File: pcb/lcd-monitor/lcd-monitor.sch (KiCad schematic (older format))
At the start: 51 parts

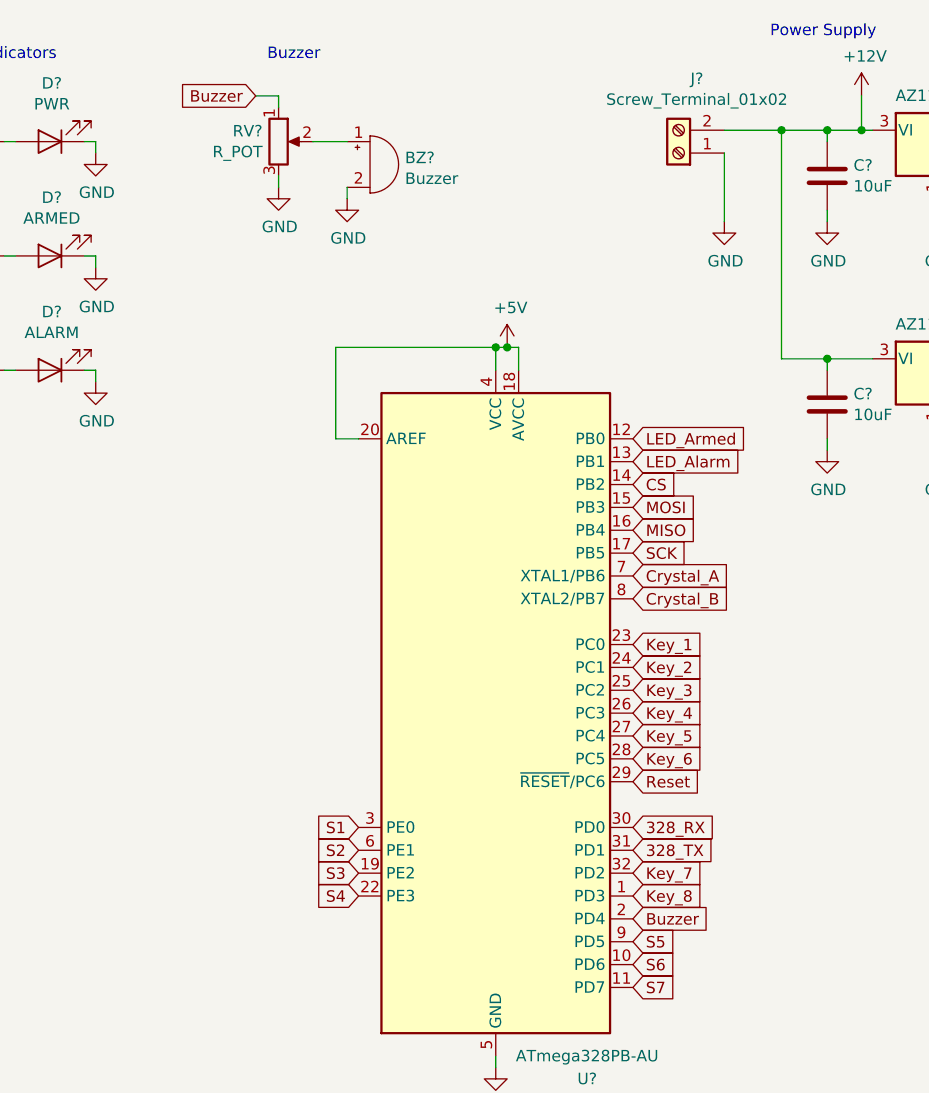
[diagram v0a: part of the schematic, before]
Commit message: Buzzer through PWM
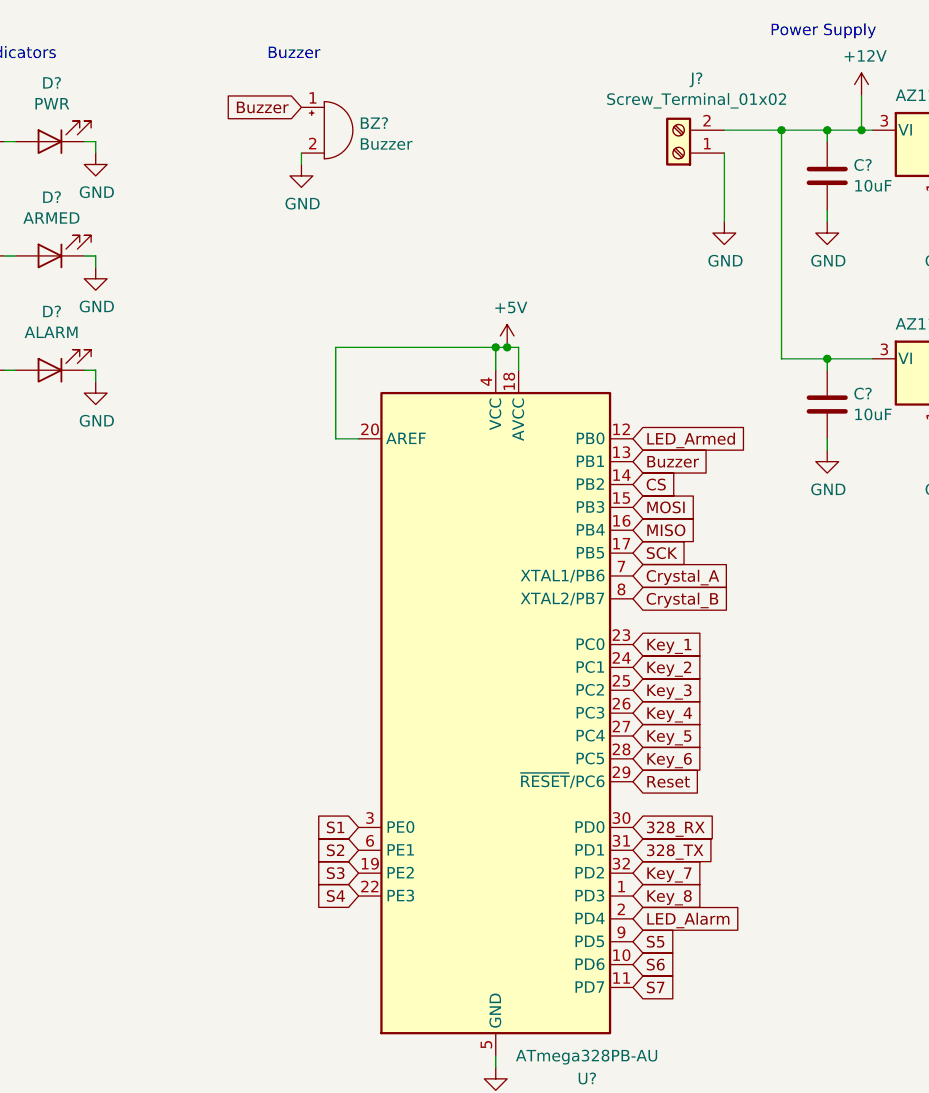
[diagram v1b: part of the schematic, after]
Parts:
- removed RV?: R_POT, symbol Device:R_POT
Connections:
- net Buzzer: now also BZ?.1 (-), U?.13 (PB1); no longer U?.2 (PD4)
- net LED_Alarm: now also U?.2 (PD4); no longer U?.13 (PB1)
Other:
- moved on the sheet: BZ?
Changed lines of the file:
@@
 Text GLabel 6350 2400 2    50   Input ~ 0
 LED_Armed
-Text GLabel 6350 2500 2    50   Input ~ 0
+Text GLabel 6350 4500 2    50   Input ~ 0
 LED_Alarm
 $Comp
 L Device:Buzzer BZ?
 U 1 1 5BD13CCE
-P 5200 1200
-F 0 "BZ?" H 5353 1229 50  0000 L CNN
-F 1 "Buzzer" H 5353 1138 50  0000 L CNN
-F 2 "" V 5175 1300 50  0001 C CNN
-F 3 "~" V 5175 1300 50  0001 C CNN
-	1    5200 1200
-	1    0    0    -1
-$EndComp
-$Comp
-L Device:R_POT RV?
-U 1 1 5BD13EFC
-P 4800 1100
-F 0 "RV?" H 4730 1146 50  0000 R CNN
-F 1 "R_POT" H 4730 1055 50  0000 R CNN
-F 2 "" H 4800 1100 50  0001 C CNN
-F 3 "~" H 4800 1100 50  0001 C CNN
-	1    4800 1100
+P 5000 1050
+F 0 "BZ?" H 5153 1079 50  0000 L CNN
+F 1 "Buzzer" H 5153 988 50  0000 L CNN
+F 2 "" V 4975 1150 50  0001 C CNN
+F 3 "~" V 4975 1150 50  0001 C CNN
+	1    5000 1050
 	1    0    0    -1
 $EndComp
 Text Notes 4750 750  0    50   ~ 0
 Buzzer
-Wire Wire Line
-	4800 950  4800 900
-Wire Wire Line
-	4950 1100 5100 1100
 $Comp
 L power:GND #PWR?
 U 1 1 5BD31A45
-P 5100 1350
-F 0 "#PWR?" H 5100 1100 50  0001 C CNN
-F 1 "GND" H 5105 1177 50  0000 C CNN
-F 2 "" H 5100 1350 50  0001 C CNN
-F 3 "" H 5100 1350 50  0001 C CNN
-	1    5100 1350
-	1    0    0    -1
-$EndComp
-$Comp
-L power:GND #PWR?
-U 1 1 5BD31A8A
-P 4800 1300
-F 0 "#PWR?" H 4800 1050 50  0001 C CNN
-F 1 "GND" H 4805 1127 50  0000 C CNN
-F 2 "" H 4800 1300 50  0001 C CNN
-F 3 "" H 4800 1300 50  0001 C CNN
-	1    4800 1300
+P 4900 1200
+F 0 "#PWR?" H 4900 950 50  0001 C CNN
+F 1 "GND" H 4905 1027 50  0000 C CNN
+F 2 "" H 4900 1200 50  0001 C CNN
+F 3 "" H 4900 1200 50  0001 C CNN
+	1    4900 1200
 	1    0    0    -1
 $EndComp
 Wire Wire Line
-	4800 1300 4800 1250
-Wire Wire Line
-	5100 1350 5100 1300
-Text GLabel 4700 900  0    50   Input ~ 0
+	4900 1200 4900 1150
+Text GLabel 4900 950  0    50   Input ~ 0
 Buzzer
-Wire Wire Line
-	4700 900  4800 900
-Text GLabel 6350 4500 2    50   Input ~ 0
+Text GLabel 6350 2500 2    50   Input ~ 0
 Buzzer
 NoConn ~ 2050 1100

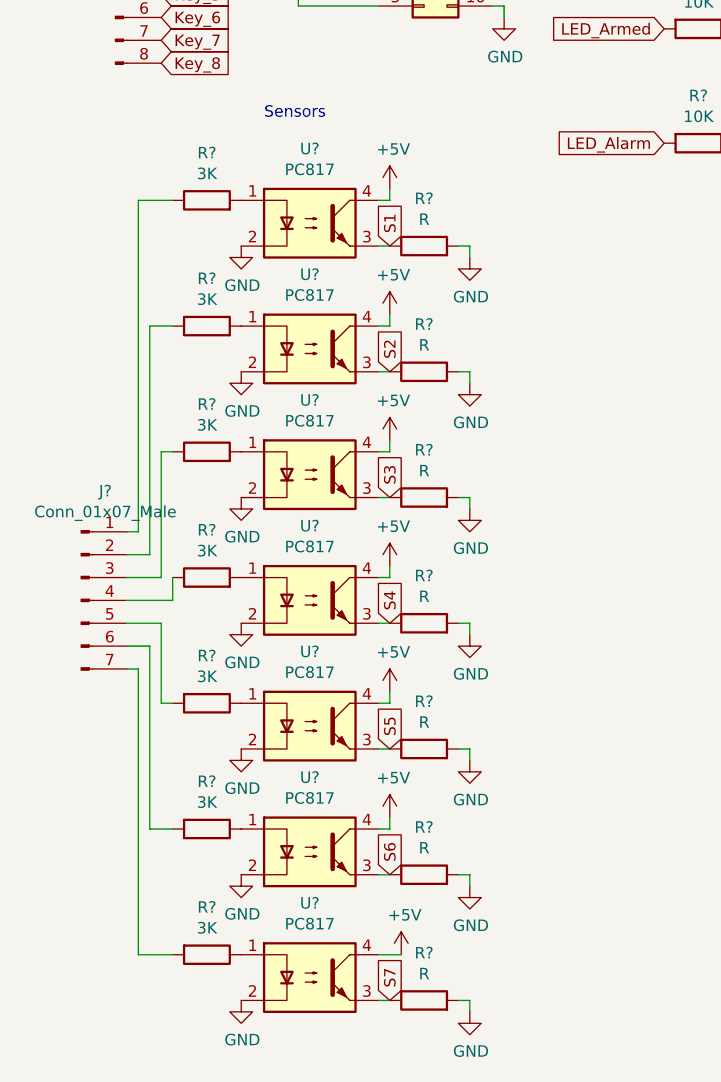
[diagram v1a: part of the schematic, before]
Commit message: Fix Optocoupler Resistor Values
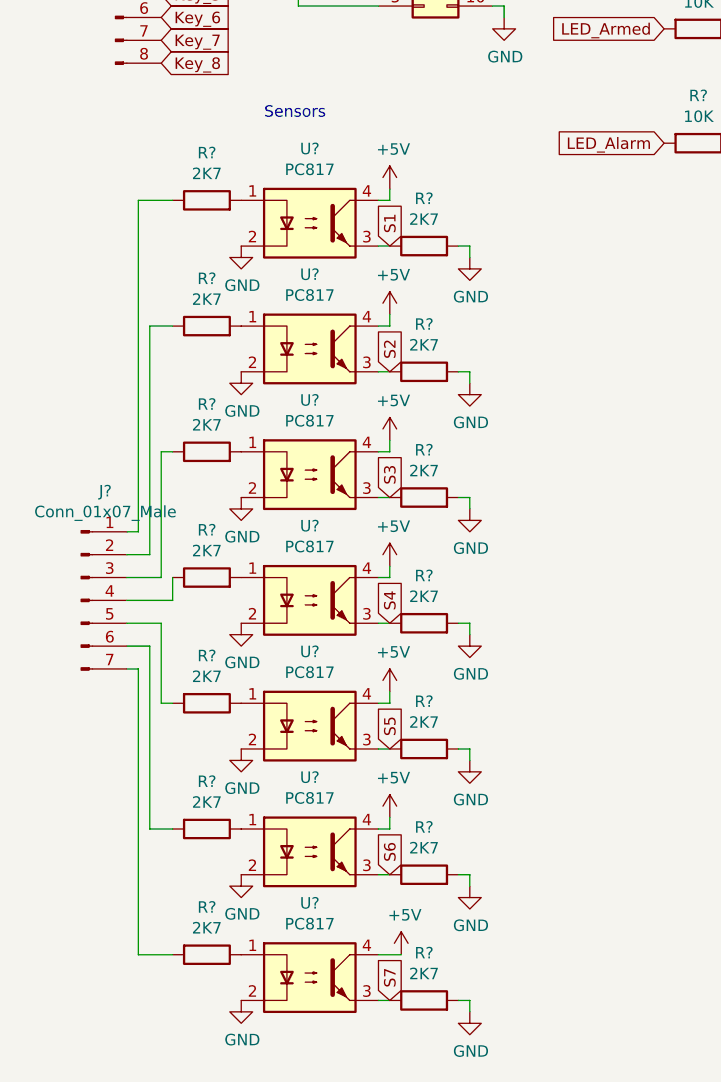
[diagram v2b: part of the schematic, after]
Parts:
- R? (x7): value R -> 2K7
- R? (x7): value 3K -> 2K7
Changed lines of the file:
@@
 P 2250 5850
 F 0 "R?" V 2457 5850 50  0000 C CNN
-F 1 "R" V 2366 5850 50  0000 C CNN
+F 1 "2K7" V 2366 5850 50  0000 C CNN
 F 2 "" V 2180 5850 50  0001 C CNN
 F 3 "~" H 2250 5850 50  0001 C CNN
@@
 P 2250 5300
 F 0 "R?" V 2457 5300 50  0000 C CNN
-F 1 "R" V 2366 5300 50  0000 C CNN
+F 1 "2K7" V 2366 5300 50  0000 C CNN
 F 2 "" V 2180 5300 50  0001 C CNN
 F 3 "~" H 2250 5300 50  0001 C CNN
@@
 P 1300 5650
 F 0 "R?" V 1093 5650 50  0000 C CNN
-F 1 "3K" V 1184 5650 50  0000 C CNN
+F 1 "2K7" V 1184 5650 50  0000 C CNN
 F 2 "" V 1230 5650 50  0001 C CNN
 F 3 "~" H 1300 5650 50  0001 C CNN
@@
 P 1300 5100
 F 0 "R?" V 1093 5100 50  0000 C CNN
-F 1 "3K" V 1184 5100 50  0000 C CNN
+F 1 "2K7" V 1184 5100 50  0000 C CNN
 F 2 "" V 1230 5100 50  0001 C CNN
 F 3 "~" H 1300 5100 50  0001 C CNN
@@
 P 1300 4550
 F 0 "R?" V 1093 4550 50  0000 C CNN
-F 1 "3K" V 1184 4550 50  0000 C CNN
+F 1 "2K7" V 1184 4550 50  0000 C CNN
 F 2 "" V 1230 4550 50  0001 C CNN
 F 3 "~" H 1300 4550 50  0001 C CNN
@@
 P 1300 4000
 F 0 "R?" V 1507 4000 50  0000 C CNN
-F 1 "3K" V 1416 4000 50  0000 C CNN
+F 1 "2K7" V 1416 4000 50  0000 C CNN
 F 2 "" V 1230 4000 50  0001 C CNN
 F 3 "~" H 1300 4000 50  0001 C CNN
@@
 P 1300 3450
 F 0 "R?" V 1507 3450 50  0000 C CNN
-F 1 "3K" V 1416 3450 50  0000 C CNN
+F 1 "2K7" V 1416 3450 50  0000 C CNN
 F 2 "" V 1230 3450 50  0001 C CNN
 F 3 "~" H 1300 3450 50  0001 C CNN
@@
 P 1300 2900
 F 0 "R?" V 1507 2900 50  0000 C CNN
-F 1 "3K" V 1416 2900 50  0000 C CNN
+F 1 "2K7" V 1416 2900 50  0000 C CNN
 F 2 "" V 1230 2900 50  0001 C CNN
 F 3 "~" H 1300 2900 50  0001 C CNN
@@
 P 1300 2350
 F 0 "R?" V 1507 2350 50  0000 C CNN
-F 1 "3K" V 1416 2350 50  0000 C CNN
+F 1 "2K7" V 1416 2350 50  0000 C CNN
 F 2 "" V 1230 2350 50  0001 C CNN
 F 3 "~" H 1300 2350 50  0001 C CNN
@@
 P 2250 4750
 F 0 "R?" V 2457 4750 50  0000 C CNN
-F 1 "R" V 2366 4750 50  0000 C CNN
+F 1 "2K7" V 2366 4750 50  0000 C CNN
 F 2 "" V 2180 4750 50  0001 C CNN
 F 3 "~" H 2250 4750 50  0001 C CNN
@@
 P 2250 4200
 F 0 "R?" V 2457 4200 50  0000 C CNN
-F 1 "R" V 2366 4200 50  0000 C CNN
+F 1 "2K7" V 2366 4200 50  0000 C CNN
 F 2 "" V 2180 4200 50  0001 C CNN
 F 3 "~" H 2250 4200 50  0001 C CNN
@@
 P 2250 3650
 F 0 "R?" V 2457 3650 50  0000 C CNN
-F 1 "R" V 2366 3650 50  0000 C CNN
+F 1 "2K7" V 2366 3650 50  0000 C CNN
 F 2 "" V 2180 3650 50  0001 C CNN
 F 3 "~" H 2250 3650 50  0001 C CNN
@@
 P 2250 3100
 F 0 "R?" V 2457 3100 50  0000 C CNN
-F 1 "R" V 2366 3100 50  0000 C CNN
+F 1 "2K7" V 2366 3100 50  0000 C CNN
 F 2 "" V 2180 3100 50  0001 C CNN
 F 3 "~" H 2250 3100 50  0001 C CNN
@@
 P 2250 2550
 F 0 "R?" V 2457 2550 50  0000 C CNN
-F 1 "R" V 2366 2550 50  0000 C CNN
+F 1 "2K7" V 2366 2550 50  0000 C CNN
 F 2 "" V 2180 2550 50  0001 C CNN
 F 3 "~" H 2250 2550 50  0001 C CNN

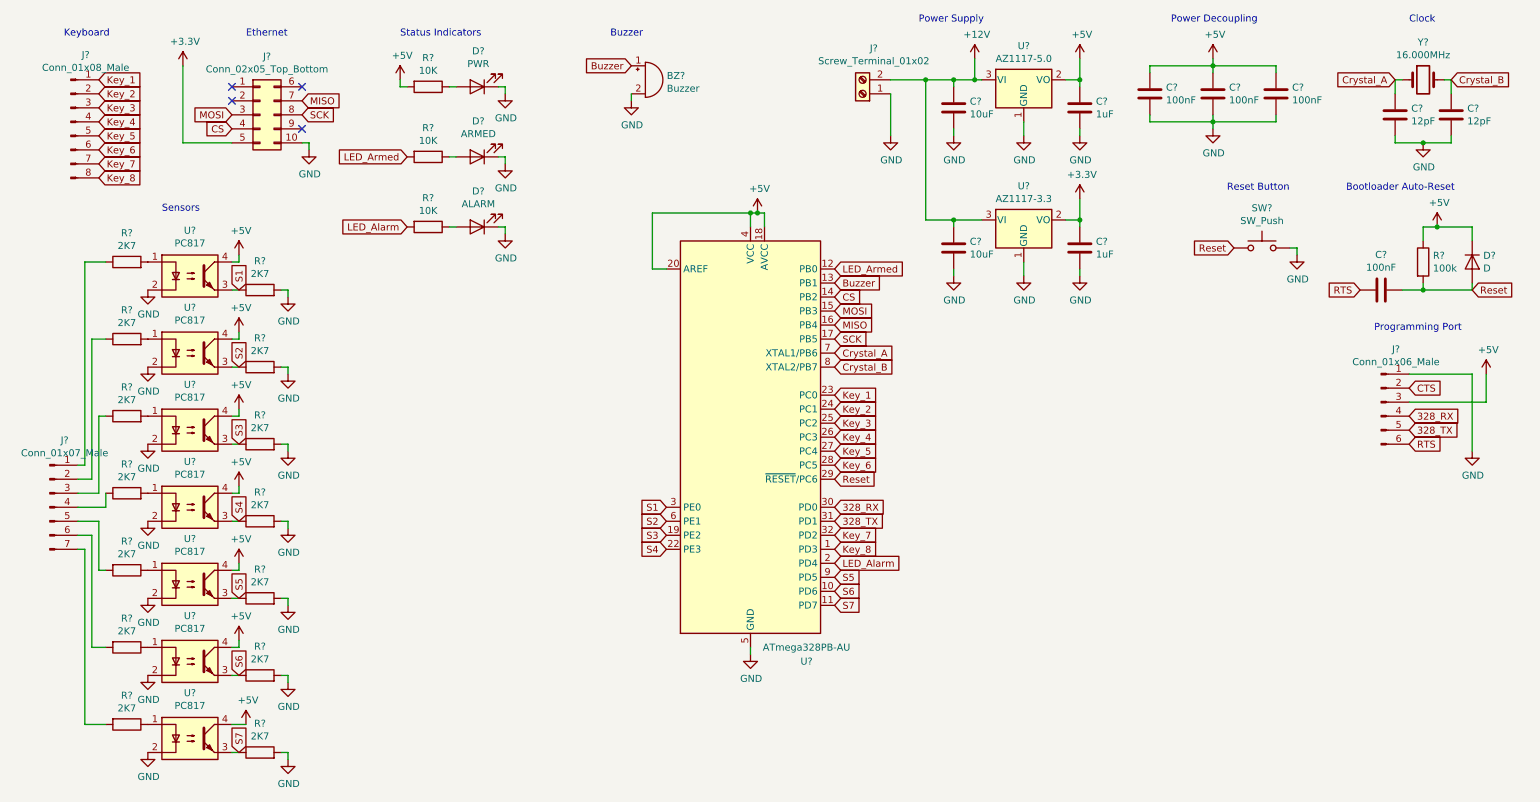
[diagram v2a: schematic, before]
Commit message: Assign Footprints
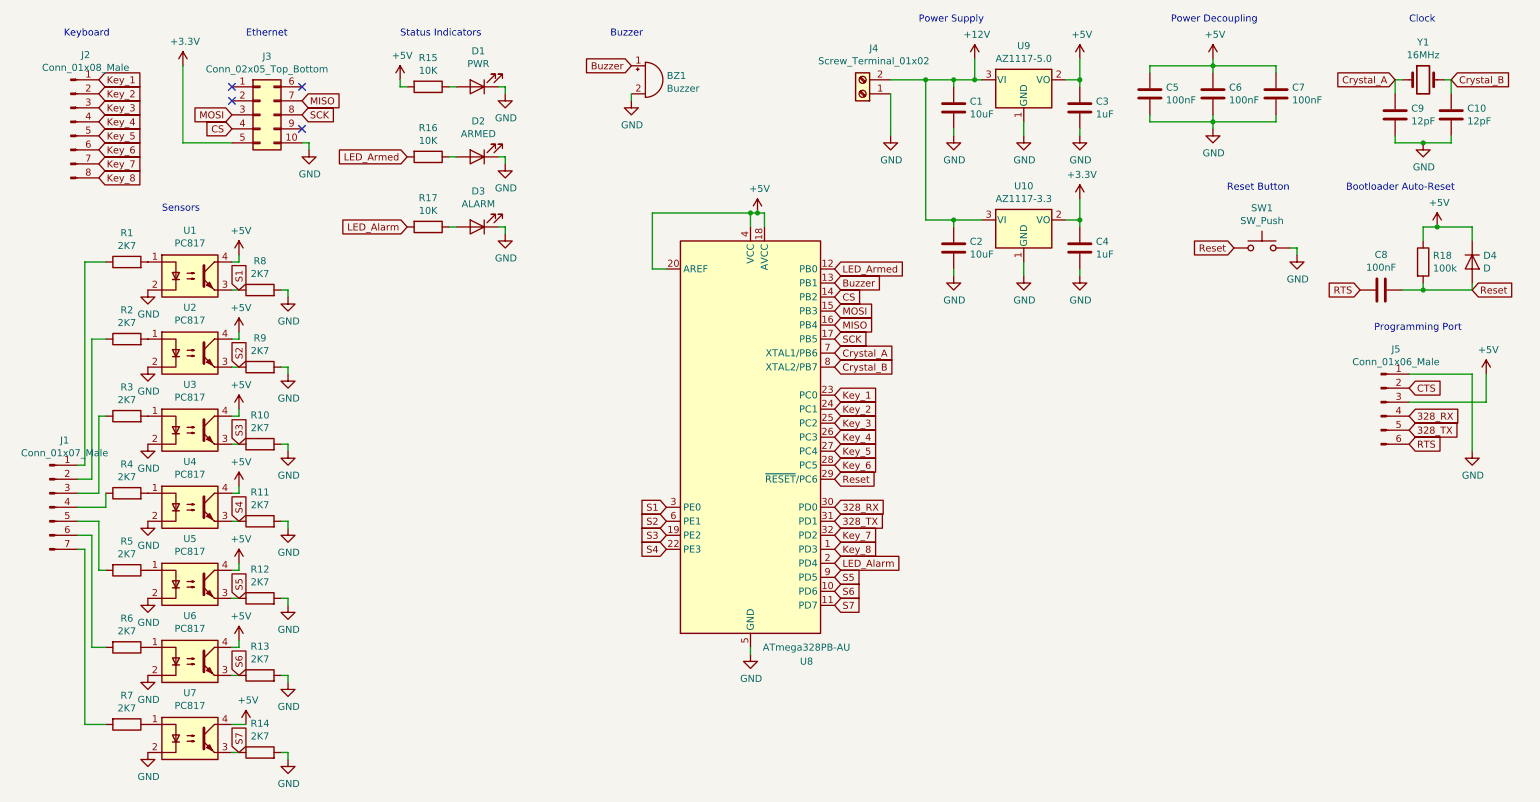
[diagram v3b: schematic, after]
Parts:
- BZ1: renamed from BZ?; footprint (none) -> Buzzer_Beeper:Buzzer_12x9.5RM7.6
- C1, C10, C2, C3, C4, C5, C6, C7, C8, C9: renamed from C?; footprint (none) -> Capacitor_SMD:C_0805_2012Metric
- D1, D2, D3: renamed from D?; footprint (none) -> LED_SMD:LED_0805_2012Metric
- D4: renamed from D?; footprint (none) -> Diode_SMD:D_0805_2012Metric
- J1: renamed from J?; footprint (none) -> Connector_PinHeader_2.54mm:PinHeader_1x07_P2.54mm_Vertical
- J2: renamed from J?; footprint (none) -> Connector_PinHeader_2.54mm:PinHeader_1x08_P2.54mm_Vertical
- J3: renamed from J?; footprint (none) -> Connector_PinSocket_2.54mm:PinSocket_2x05_P2.54mm_Vertical
- J4: renamed from J?; footprint (none) -> TerminalBlock:TerminalBlock_Altech_AK300-2_P5.00mm
- J5: renamed from J?; footprint (none) -> Connector_PinHeader_2.54mm:PinHeader_1x06_P2.54mm_Vertical
- R1, R10, R11, R12, R13, R14, R15, R16, R17, R18, R2, R3, R4, R5, R6, R7, R8, R9: renamed from R?; footprint (none) -> Resistor_SMD:R_0805_2012Metric
- SW1: renamed from SW?; footprint (none) -> Button_Switch_SMD:SW_SPST_FSMSM
- U10, U9: renamed from U?; footprint (none) -> Package_TO_SOT_SMD:SOT-223
- Y1: renamed from Y?; value 16.000MHz -> 16MHz; footprint (none) -> Crystal:Crystal_SMD_3225-4Pin_3.2x2.5mm
- gave numbers to parts that had none: 8

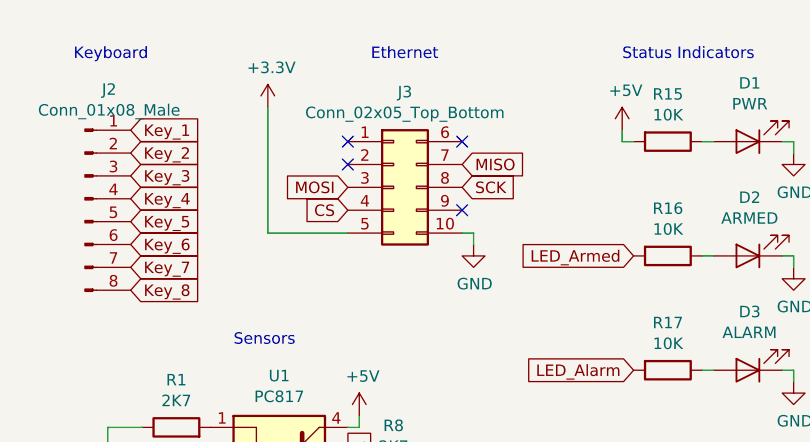
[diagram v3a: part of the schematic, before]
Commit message: Fix Ethernet Header
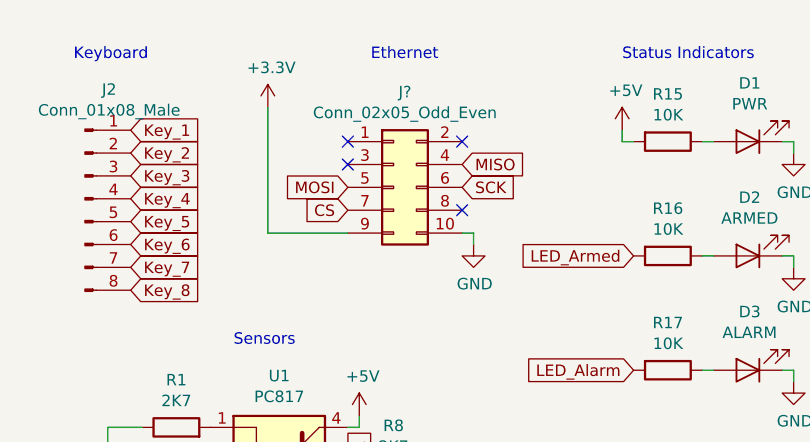
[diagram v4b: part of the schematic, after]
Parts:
- removed J3: Conn_02x05_Top_Bottom, Connector_PinSocket_2.54mm:PinSocket_2x05_P2.54mm_Vertical, symbol Connector_Generic:Conn_02x05_Top_Bottom
- added J?: Conn_02x05_Odd_Even, symbol Connector_Generic:Conn_02x05_Odd_Even
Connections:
- net +3V3: now also J?.9 (Pin_9)
- net CS: now also J?.7 (Pin_7)
- net GND: now also J?.10 (Pin_10)
- net MISO: now also J?.4 (Pin_4)
- net MOSI: now also J?.5 (Pin_5)
- net SCK: now also J?.6 (Pin_6)
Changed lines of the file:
@@
-	1    0    0    -1
-$EndComp
-$Comp
-L Connector_Generic:Conn_02x05_Top_Bottom J3
-U 1 1 5BCD4619
-P 2250 1300
-F 0 "J3" H 2300 1717 50  0000 C CNN
-F 1 "Conn_02x05_Top_Bottom" H 2300 1626 50  0000 C CNN
-F 2 "Connector_PinSocket_2.54mm:PinSocket_2x05_P2.54mm_Vertical" H 2250 1300 50  0001 C CNN
-F 3 "~" H 2250 1300 50  0001 C CNN
-	1    2250 1300
 	1    0    0    -1
 $EndComp
@@
 Text GLabel 5150 4300 0    50   Input ~ 0
 S3
+$Comp
+L Connector_Generic:Conn_02x05_Odd_Even J?
+U 1 1 5BCAAB4F
+P 2250 1300
+F 0 "J?" H 2300 1717 50  0000 C CNN
+F 1 "Conn_02x05_Odd_Even" H 2300 1626 50  0000 C CNN
+F 2 "" H 2250 1300 50  0001 C CNN
+F 3 "~" H 2250 1300 50  0001 C CNN
+	1    2250 1300
+	1    0    0    -1
+$EndComp
 $EndSCHEMATC
